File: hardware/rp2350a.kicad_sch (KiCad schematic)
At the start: 33 parts, among them Q26 AP1606, U10 RP2354A, U24 FXMAR2104UMX, X1 12MHz

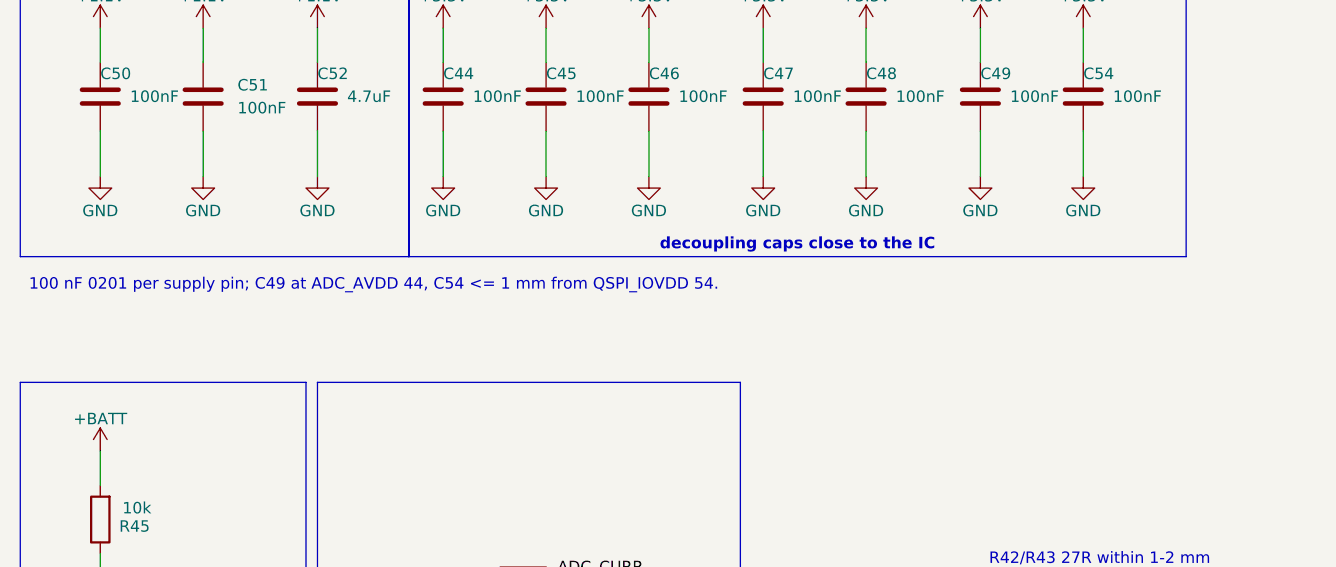
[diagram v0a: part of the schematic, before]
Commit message: Build functional floorplan with checked power loops and RF reservations
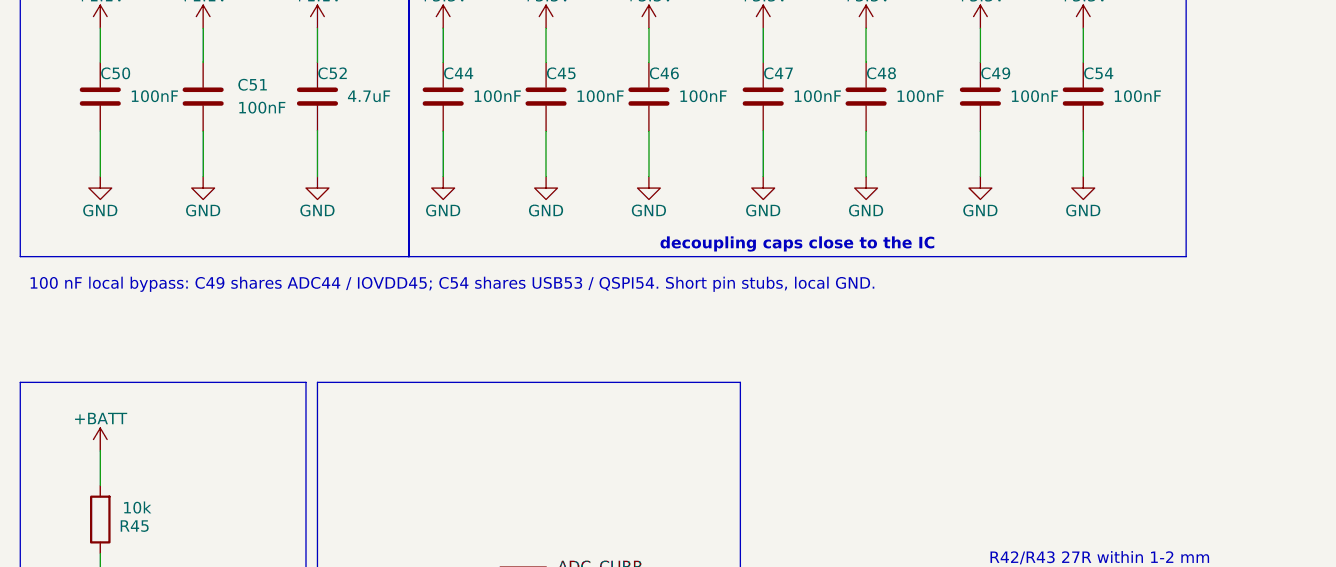
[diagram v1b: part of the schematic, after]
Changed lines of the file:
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@@
 		)
 	)
-	(text_box "100 nF 0201 per supply pin; C49 at ADC_AVDD 44, C54 <= 1 mm from QSPI_IOVDD 54."
+	(text_box "100 nF local bypass: C49 shares ADC44 / IOVDD45; C54 shares USB53 / QSPI54. Short pin stubs, local GND."
 		(exclude_from_sim no)
 		(at 91.44 73.66 0)
-		(size 129.54 7.62)
+		(size 144.78 7.62)
 		(margins 0.9525 0.9525 0.9525 0.9525)
 		(stroke

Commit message: Route four DShot channels and close local ground returns
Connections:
- net MOTOR1: now also U24.10 (B2); no longer U24.12 (B0)
- net MOTOR1_FC: now also U10.8 (GPIO5), U24.5 (A2); no longer U10.10 (GPIO7), U24.3 (A0)
- net MOTOR3: now also U24.12 (B0); no longer U24.10 (B2)
- net MOTOR3_FC: now also U10.10 (GPIO7), U24.3 (A0); no longer U10.8 (GPIO5), U24.5 (A2)
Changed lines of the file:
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@@
 		)
 	)
-	(label "MOTOR1_FC"
+	(label "MOTOR3_FC"
 		(at 321.31 109.22 0)
 		(effects
@@
 		)
 	)
-	(label "MOTOR1_FC"
+	(label "MOTOR3_FC"
 		(at 388.62 184.15 180)
 		(effects
@@
 		)
 	)
-	(label "MOTOR3_FC"
+	(label "MOTOR1_FC"
 		(at 388.62 189.23 180)
 		(effects
@@
 		)
 	)
-	(label "MOTOR3_FC"
+	(label "MOTOR1_FC"
 		(at 321.31 104.14 0)
 		(effects
@@
 		)
 	)
-	(hierarchical_label "MOTOR3"
+	(hierarchical_label "MOTOR1"
 		(shape bidirectional)
 		(at 429.26 189.23 0)
@@
 		)
 	)
-	(hierarchical_label "MOTOR1"
+	(hierarchical_label "MOTOR3"
 		(shape bidirectional)
 		(at 429.26 184.15 0)

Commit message: Route flash receiver controls and power entry with scoped reference checks
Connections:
- net FLASH_CS: now also U10.31 (GPIO19); no longer U10.3 (GPIO1)
- net HD_EN: now also U10.3 (GPIO1); no longer U10.31 (GPIO19)
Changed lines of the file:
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@@
 		)
 	)
-	(text_box "GPIO groups follow U10 at -90 deg: flash 0-3 east; motors 7/6/5/4 north to U24 A0-A3.\nGyro 10-15 west: INT10, MOSI11, MISO12, CLK13, SCK14, CS15. Keep this order to match U11 pads.\nUART0 16/17; strip18; HD_EN19; buzzer20. OSD21-23 and CRSF24/25 south. ADC26/27; spare28/29. LEDs8/9."
+	(text_box "GPIO assignments: SPI0 MISO0, SCK2, MOSI3; software flash CS19. HD_EN1. Motors 5/6/7/4 map to motors 1/2/3/4.\nGyro: INT10, MOSI11, MISO12, CLK13, SCK14, CS15. Preserve the verified SPI mux and U11 pad order.\nReceiver UART0 16/17; HD UART1 24/25; strip18; buzzer20; OSD W21/EN22/SYNC23; LEDs8/9.\nADC current26/battery27. GPIO28/29 are unconnected in this schematic. Read physical escape directions from the saved PCB."
 		(exclude_from_sim no)
 		(at 353.06 129.54 0)
@@
 		)
 	)
-	(hierarchical_label "HD_EN"
+	(hierarchical_label "FLASH_CS"
 		(shape output)
 		(at 321.31 154.94 0)
@@
 		)
 	)
-	(hierarchical_label "FLASH_CS"
+	(hierarchical_label "HD_EN"
 		(shape output)
 		(at 321.31 90.17 0)

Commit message: Complete power and local control routes with reference repair
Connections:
- net LED_STRIP: now also U10.43 (GPIO29_ADC3); no longer U10.29 (GPIO18)
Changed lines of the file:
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@@
 		)
 	)
-	(text_box "GPIO assignments: SPI0 MISO0, SCK2, MOSI3; software flash CS19. HD_EN1. Motors 5/6/7/4 map to motors 1/2/3/4.\nGyro: INT10, MOSI11, MISO12, CLK13, SCK14, CS15. Preserve the verified SPI mux and U11 pad order.\nReceiver UART0 16/17; HD UART1 24/25; strip18; buzzer20; OSD W21/EN22/SYNC23; LEDs8/9.\nADC current26/battery27. GPIO28/29 are unconnected in this schematic. Read physical escape directions from the saved PCB."
+	(text_box "GPIO assignments: SPI0 MISO0, SCK2, MOSI3; software flash CS19. HD_EN1. Motors 5/6/7/4 map to motors 1/2/3/4.\nGyro: INT10, MOSI11, MISO12, CLK13, SCK14, CS15. Preserve the verified SPI mux and U11 pad order.\nReceiver UART0 16/17; HD UART1 24/25; strip29; buzzer20; OSD W21/EN22/SYNC23; LEDs8/9.\nADC current26/battery27. GPIO18/28 are unconnected in this schematic. Read physical escape directions from the saved PCB."
 		(exclude_from_sim no)
 		(at 353.06 129.54 0)
@@
 	)
 	(no_connect
-		(at 321.31 191.77)
+		(at 321.31 152.4)
 	)
 	(no_connect
@@
 	(hierarchical_label "LED_STRIP"
 		(shape output)
-		(at 321.31 152.4 0)
-		(effects
-			(font
+		(at 321.31 191.77 0)
+		(effects
+			(font
